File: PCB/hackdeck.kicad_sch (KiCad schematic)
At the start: 13 parts, among them SW1 SW_Push, SW2 SW_Push, SW3 SW_Push, SW4 SW_Push, SW5 RotaryEncoder, SW6 SW_Push, SW7 SW_Push, U1 XIAO-RP2040-DIP, U2 OLED

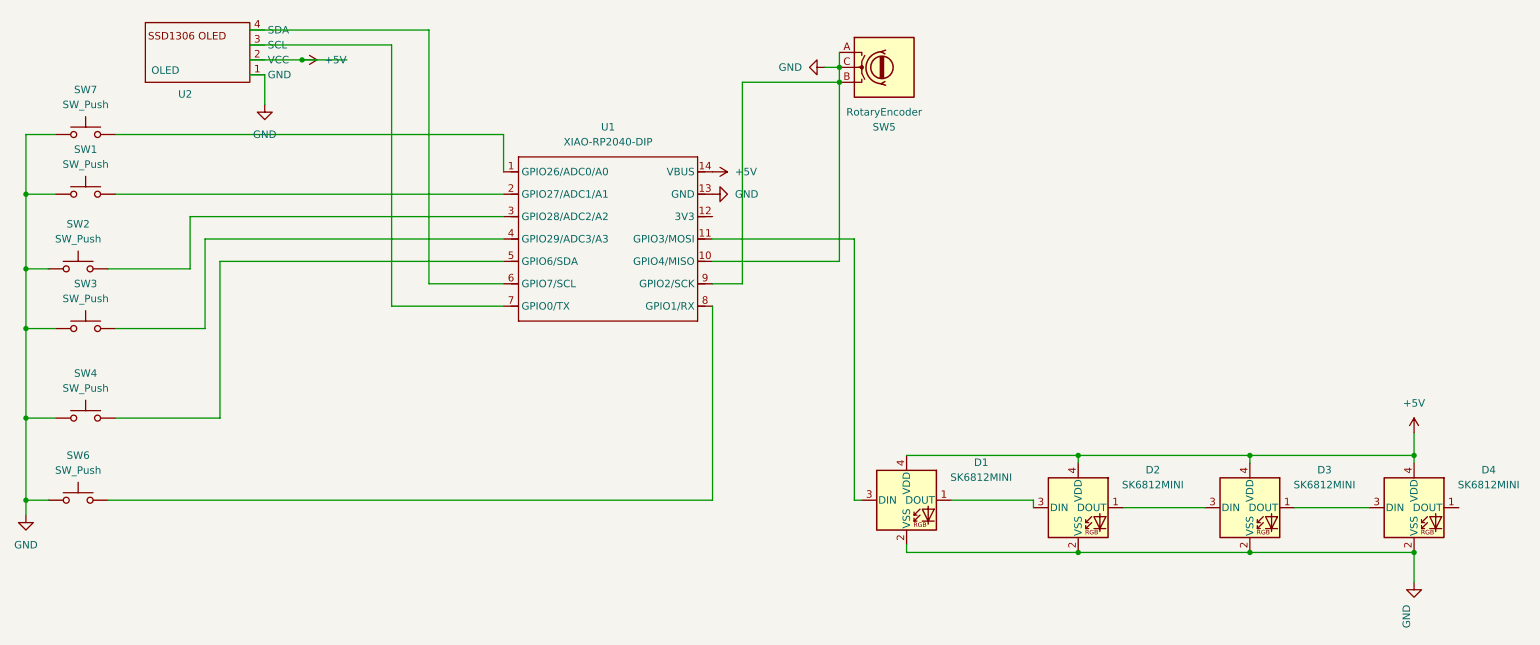
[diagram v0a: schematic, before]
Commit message: OLED and Rotary fix
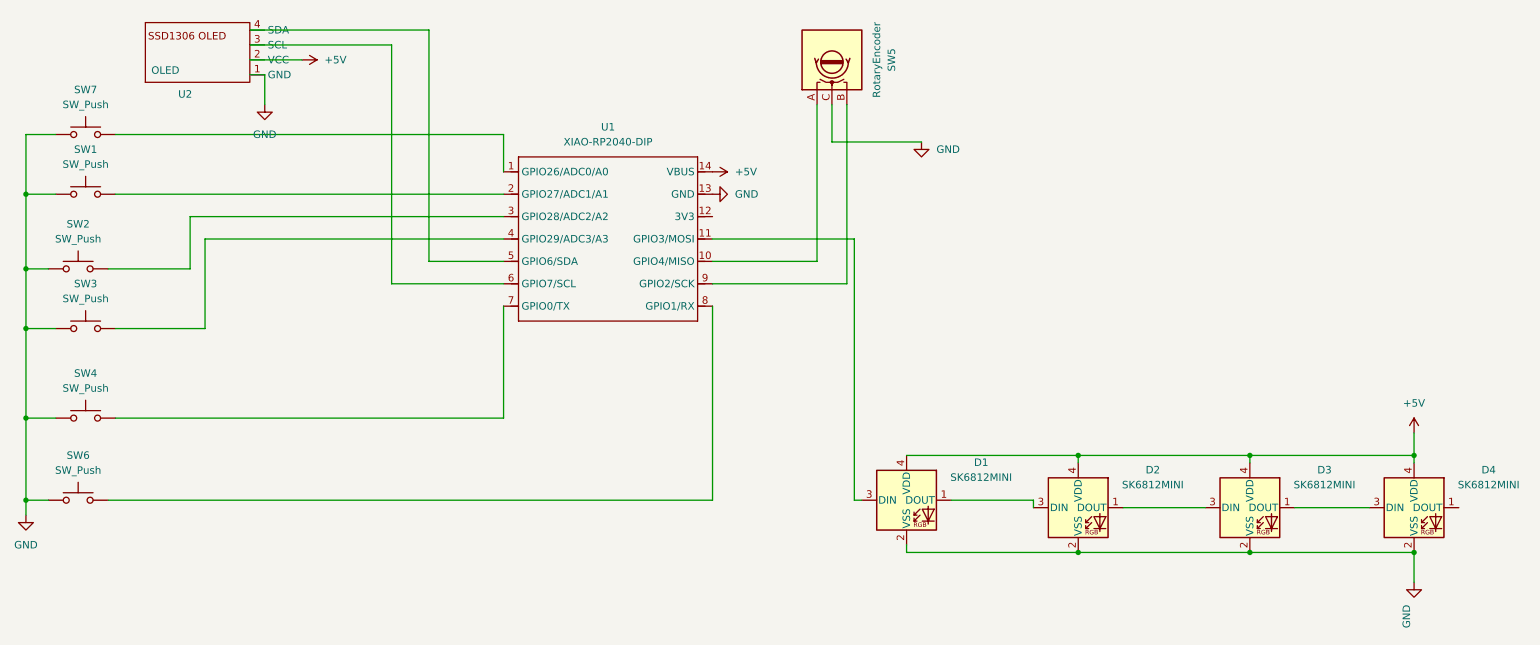
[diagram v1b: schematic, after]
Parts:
- U1: footprint OPL:XIAO-RP2040-DIP -> XIAO:XIAO-RP2040-DIP
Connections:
- net GND: no longer SW5.A, SW5.B, U1.10 (GPIO4/MISO), U1.9 (GPIO2/SCK)
- net at U1.5 (GPIO6/SDA): now also U2.4 (SDA); no longer SW4.2
- net at U1.6 (GPIO7/SCL): now also U2.3 (SCL); no longer U2.4 (SDA)
- net at U1.7 (GPIO0/TX): now also SW4.2; no longer U2.3 (SCL)
- new net: SW5.A, U1.10 (GPIO4/MISO)
- new net: SW5.B, U1.9 (GPIO2/SCK)
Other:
- moved on the sheet: SW5
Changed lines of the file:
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@@
-	)
-	(junction
-		(at 73.66 35.56)
-		(diameter 0)
-		(color 0 0 0 0)
-	)
-	(junction
-		(at 165.1 36.83)
-		(diameter 0)
-		(color 0 0 0 0)
 	)
 	(junction
@@
 	)
 	(junction
-		(at 165.1 39.37)
-		(diameter 0)
-		(color 0 0 0 0)
-	)
-	(junction
 		(at 26.67 58.42)
 		(diameter 0)
@@
 	(wire
 		(pts
-			(xy 148.59 39.37) (xy 148.59 73.66)
-		)
-		(stroke
-			(width 0)
-			(type default)
-		)
-	)
-	(wire
-		(pts
 			(xy 40.64 110.49) (xy 143.51 110.49)
 		)
@@
 	(wire
 		(pts
-			(xy 59.69 69.85) (xy 107.95 69.85)
+			(xy 166.37 43.18) (xy 166.37 73.66)
 		)
 		(stroke
@@
 	(wire
 		(pts
+			(xy 95.25 69.85) (xy 107.95 69.85)
+		)
+		(stroke
+			(width 0)
+			(type default)
+		)
+	)
+	(wire
+		(pts
 			(xy 67.31 43.18) (xy 67.31 38.1)
 		)
@@
 	(wire
 		(pts
-			(xy 165.1 39.37) (xy 148.59 39.37)
+			(xy 88.9 33.02) (xy 88.9 73.66)
 		)
 		(stroke
@@
 	(wire
 		(pts
+			(xy 143.51 73.66) (xy 166.37 73.66)
+		)
+		(stroke
+			(width 0)
+			(type default)
+		)
+	)
+	(wire
+		(pts
 			(xy 262.89 102.87) (xy 262.89 104.14)
 		)
@@
 	(wire
 		(pts
+			(xy 95.25 30.48) (xy 95.25 69.85)
+		)
+		(stroke
+			(width 0)
+			(type default)
+		)
+	)
+	(wire
+		(pts
 			(xy 57.15 81.28) (xy 57.15 66.04)
 		)
@@
 	(wire
 		(pts
-			(xy 165.1 34.29) (xy 165.1 36.83)
+			(xy 163.83 43.18) (xy 163.83 49.53)
 		)
 		(stroke
@@
 	(wire
 		(pts
-			(xy 95.25 30.48) (xy 95.25 73.66)
-		)
-		(stroke
-			(width 0)
-			(type default)
-		)
-	)
-	(wire
-		(pts
 			(xy 67.31 38.1) (xy 64.77 38.1)
 		)
@@
 	(wire
 		(pts
+			(xy 143.51 69.85) (xy 161.29 69.85)
+		)
+		(stroke
+			(width 0)
+			(type default)
+		)
+	)
+	(wire
+		(pts
 			(xy 184.15 110.49) (xy 198.12 110.49)
 		)
@@
 	(wire
 		(pts
-			(xy 88.9 33.02) (xy 88.9 77.47)
-		)
-		(stroke
-			(width 0)
-			(type default)
-		)
-	)
-	(wire
-		(pts
 			(xy 167.64 66.04) (xy 143.51 66.04)
 		)
@@
 	(wire
 		(pts
-			(xy 81.28 35.56) (xy 73.66 35.56)
-		)
-		(stroke
-			(width 0)
-			(type default)
-		)
-	)
-	(wire
-		(pts
 			(xy 205.74 102.87) (xy 176.53 102.87)
 		)
@@
 	(wire
 		(pts
-			(xy 165.1 69.85) (xy 143.51 69.85)
-		)
-		(stroke
-			(width 0)
-			(type default)
-		)
-	)
-	(wire
-		(pts
 			(xy 26.67 110.49) (xy 26.67 113.03)
 		)
@@
 	(wire
 		(pts
-			(xy 59.69 96.52) (xy 59.69 69.85)
-		)
-		(stroke
-			(width 0)
-			(type default)
-		)
-	)
-	(wire
-		(pts
 			(xy 107.95 48.26) (xy 107.95 54.61)
 		)
@@
 	(wire
 		(pts
+			(xy 107.95 77.47) (xy 107.95 96.52)
+		)
+		(stroke
+			(width 0)
+			(type default)
+		)
+	)
+	(wire
+		(pts
 			(xy 262.89 102.87) (xy 234.95 102.87)
 		)
@@
 	(wire
 		(pts
-			(xy 148.59 73.66) (xy 143.51 73.66)
-		)
-		(stroke
-			(width 0)
-			(type default)
-		)
-	)
-	(wire
-		(pts
-			(xy 95.25 73.66) (xy 107.95 73.66)
-		)
-		(stroke
-			(width 0)
-			(type default)
-		)
-	)
-	(wire
-		(pts
 			(xy 31.75 48.26) (xy 26.67 48.26)
 		)
@@
 	(wire
 		(pts
+			(xy 88.9 73.66) (xy 107.95 73.66)
+		)
+		(stroke
+			(width 0)
+			(type default)
+		)
+	)
+	(wire
+		(pts
 			(xy 205.74 119.38) (xy 234.95 119.38)
 		)
@@
 	(wire
 		(pts
+			(xy 161.29 69.85) (xy 161.29 43.18)
+		)
+		(stroke
+			(width 0)
+			(type default)
+		)
+	)
+	(wire
+		(pts
 			(xy 242.57 111.76) (xy 255.27 111.76)
 		)
@@
 	(wire
 		(pts
-			(xy 41.91 96.52) (xy 59.69 96.52)
-		)
-		(stroke
-			(width 0)
-			(type default)
-		)
-	)
-	(wire
-		(pts
-			(xy 88.9 77.47) (xy 107.95 77.47)
-		)
-		(stroke
-			(width 0)
-			(type default)
-		)
-	)
-	(wire
-		(pts
-			(xy 165.1 36.83) (xy 162.56 36.83)
+			(xy 163.83 49.53) (xy 179.07 49.53)
 		)
 		(stroke
@@
 	(wire
 		(pts
-			(xy 165.1 39.37) (xy 165.1 69.85)
-		)
-		(stroke
-			(width 0)
-			(type default)
-		)
-	)
-	(wire
-		(pts
 			(xy 26.67 110.49) (xy 30.48 110.49)
 		)
@@
 	(wire
 		(pts
-			(xy 165.1 36.83) (xy 165.1 39.37)
-		)
-		(stroke
-			(width 0)
-			(type default)
-		)
-	)
-	(wire
-		(pts
 			(xy 26.67 71.12) (xy 26.67 81.28)
 		)
@@
 		(pts
 			(xy 26.67 58.42) (xy 31.75 58.42)
+		)
+		(stroke
+			(width 0)
+			(type default)
+		)
+	)
+	(wire
+		(pts
+			(xy 107.95 96.52) (xy 41.91 96.52)
 		)
 		(stroke
@@
 	(symbol
 		(lib_id "Device:RotaryEncoder")
-		(at 172.72 36.83 0)
+		(at 163.83 35.56 90)
 		(unit 1)
 		(exclude_from_sim no)
@@
 		(dnp no)
 		(property "Reference" "SW5"
-			(at 172.72 46.99 0)
+			(at 173.99 35.56 0)
 			(effects
 				(font
@@
 		)
 		(property "Value" "RotaryEncoder"
-			(at 172.72 44.45 0)
+			(at 171.45 35.56 0)
 			(effects
 				(font
@@
 		)
 		(property "Footprint" "Rotary_Encoder:RotaryEncoder_Alps_EC11E_Vertical_H20mm"
-			(at 168.91 32.766 0)
+			(at 159.766 39.37 0)
 			(effects
 				(font
@@
 		)
 		(property "Datasheet" "~"
-			(at 172.72 30.226 0)
+			(at 157.226 35.56 0)
 			(effects
 				(font
@@
 		)
 		(property "Description" "Rotary encoder, dual channel, incremental quadrate outputs"
-			(at 172.72 36.83 0)
+			(at 163.83 35.56 0)
 			(effects
 				(font
@@
 			)
 		)
-		(property "Footprint" "OPL:XIAO-RP2040-DIP"
+		(property "Footprint" "XIAO:XIAO-RP2040-DIP"
 			(at 126.238 81.788 0)
 			(effects
@@
 	(symbol
 		(lib_id "power:GND")
-		(at 162.56 36.83 270)
-		(mirror x)
+		(at 179.07 49.53 0)
+		(mirror y)
 		(unit 1)
 		(exclude_from_sim no)
@@
 		(fields_autoplaced yes)
 		(property "Reference" "#PWR05"
-			(at 156.21 36.83 0)
+			(at 179.07 55.88 0)
 			(effects
 				(font
@@
 		)
 		(property "Value" "GND"
-			(at 158.75 36.8301 90)
+			(at 181.61 50.7999 0)
 			(effects
 				(font
@@
 		)
 		(property "Footprint" ""
-			(at 162.56 36.83 0)
+			(at 179.07 49.53 0)
 			(effects
 				(font
@@
 		)
 		(property "Datasheet" ""
-			(at 162.56 36.83 0)
+			(at 179.07 49.53 0)
 			(effects
 				(font
@@
 		)
 		(property "Description" "Power symbol creates a global label with name \"GND\" , ground"
-			(at 162.56 36.83 0)
-			(effects
-				(font
+			(at 179.07 49.53 0)
+			(effects
+				(font
